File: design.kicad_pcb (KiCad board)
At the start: 2 copper layers, 60.2 x 62 mm, 32 parts, among them J1 USB_A, J2 HRO_TYPE-C-31-M-12, J3 USB_A, SW1 EN, SW2 IO9, U1 AP22804AW5, U2 AP22804AW5, U3 ESP32-C3-WROOM-02-N4, U4 MCP1700T-3302E

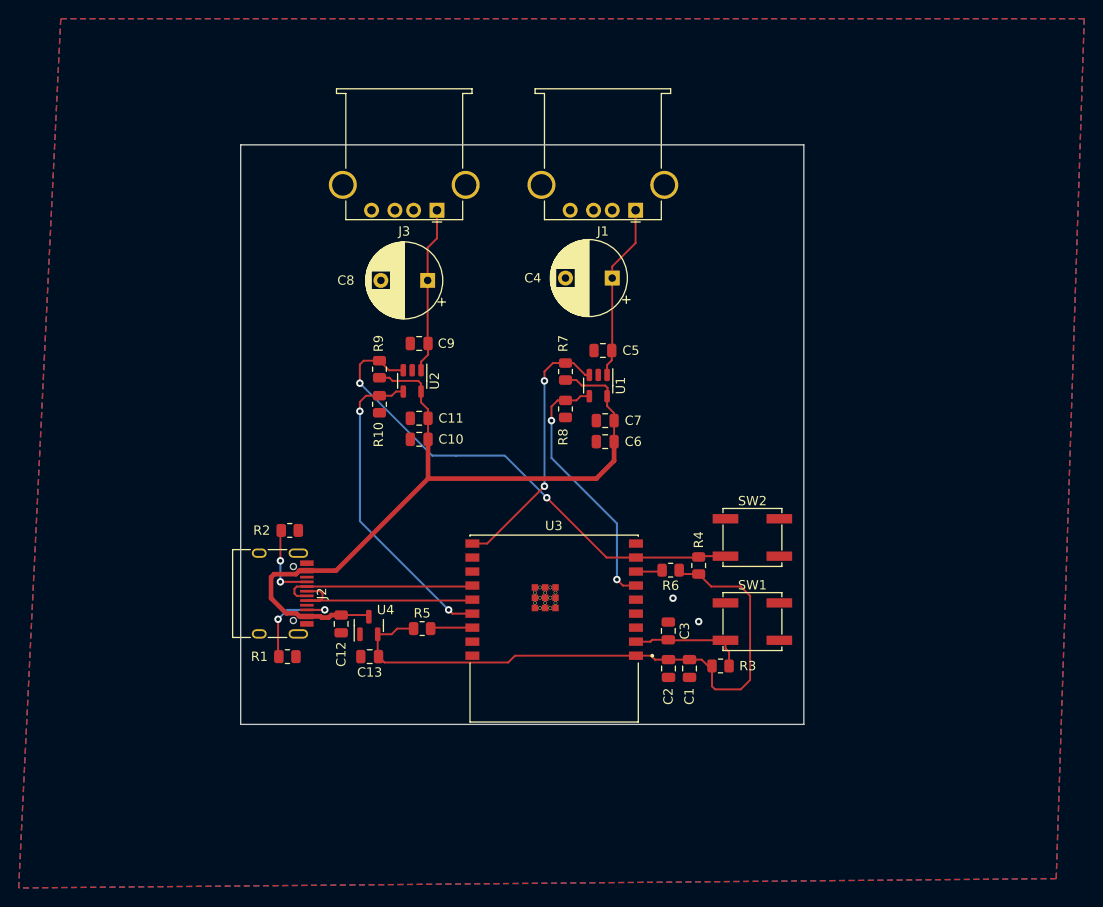
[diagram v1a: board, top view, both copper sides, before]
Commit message: add back variables for CI, rounded corners, mounting holes
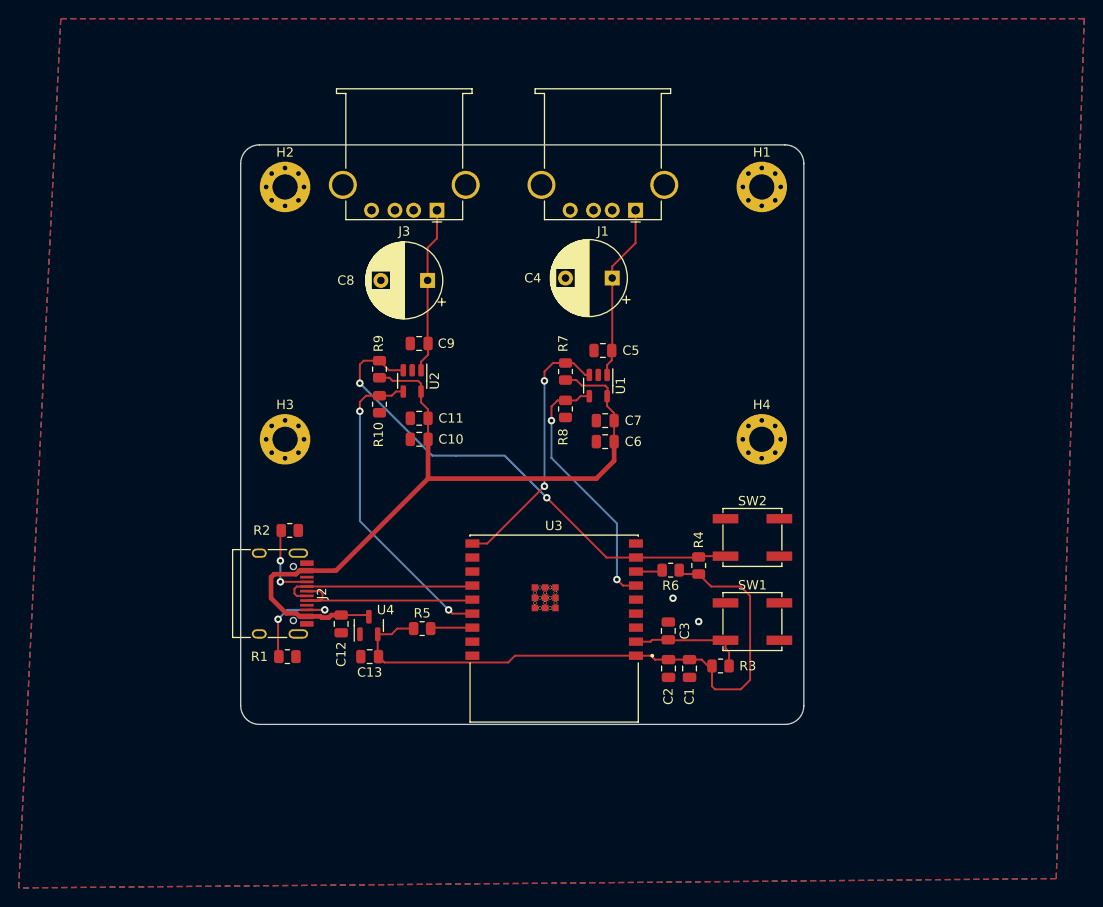
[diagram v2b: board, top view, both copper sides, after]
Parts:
- added H1: MountingHole, MountingHole:MountingHole_2.7mm_M2.5_Pad_Via, F.Cu at (180.0, 88.0)
- added H2: MountingHole, MountingHole:MountingHole_2.7mm_M2.5_Pad_Via, F.Cu at (129.0, 88.0)
- added H3: MountingHole, MountingHole:MountingHole_2.7mm_M2.5_Pad_Via, F.Cu at (129.0, 115.0)
- added H4: MountingHole, MountingHole:MountingHole_2.7mm_M2.5_Pad_Via, F.Cu at (180.0, 115.0)
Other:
- outline, holes or cut-outs redrawn
- board text added: "<<project_name>> <<ID>> <<version>> <<date>> <<hash>> <<website_link>>"
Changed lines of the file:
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@@
     )
+  )
+  (footprint "MountingHole:MountingHole_2.7mm_M2.5_Pad_Via" (layer "F.Cu")
+    (at 180 88)
+    (descr "Mounting Hole 2.7mm")
+    (tags "mounting hole 2.7mm")
+    (property "Sheetfile" "design.kicad_sch")
+    (property "Sheetname" "")
+    (attr exclude_from_pos_files)
+    (fp_text reference "H1" (at 0 -3.7) (layer "F.SilkS")
+      (effects (font (size 1 1) (thickness 0.15)))
+    )
+    (fp_text value "MountingHole" (at 0 3.7) (layer "F.Fab")
+      (effects (font (size 1 1) (thickness 0.15)))
+    )
+    (fp_text user "${REFERENCE}" (at 0 0) (layer "F.Fab")
+      (effects (font (size 1 1) (thickness 0.15)))
+    )
+    (fp_circle (center 0 0) (end 2.7 0) (layer "Cmts.User") (width 0.15) (fill none))
+    (fp_circle (center 0 0) (end 2.95 0) (layer "F.CrtYd") (width 0.05) (fill none))
+    (pad "1" thru_hole circle (at -1.431891 1.431891) (size 0.8 0.8) (drill 0.5) (layers *.Cu *.Mask))
+    (pad "1" thru_hole circle (at 2.025 0) (size 0.8 0.8) (drill 0.5) (layers *.Cu *.Mask))
+    (pad "1" thru_hole circle (at 1.431891 -1.431891) (size 0.8 0.8) (drill 0.5) (layers *.Cu *.Mask))
+    (pad "1" thru_hole circle (at 0 2.025) (size 0.8 0.8) (drill 0.5) (layers *.Cu *.Mask))
+    (pad "1" thru_hole circle (at -2.025 0) (size 0.8 0.8) (drill 0.5) (layers *.Cu *.Mask))
+    (pad "1" thru_hole circle (at 0 0) (size 5.4 5.4) (drill 2.7) (layers *.Cu *.Mask))
+    (pad "1" thru_hole circle (at 0 -2.025) (size 0.8 0.8) (drill 0.5) (layers *.Cu *.Mask))
+    (pad "1" thru_hole circle (at -1.431891 -1.431891) (size 0.8 0.8) (drill 0.5) (layers *.Cu *.Mask))
+    (pad "1" thru_hole circle (at 1.431891 1.431891) (size 0.8 0.8) (drill 0.5) (layers *.Cu *.Mask))
   )
   (footprint "Resistor_SMD:R_0805_2012Metric" (layer "F.Cu")
@@
     )
   )
+  (footprint "MountingHole:MountingHole_2.7mm_M2.5_Pad_Via" (layer "F.Cu")
+    (at 129 115)
+    (descr "Mounting Hole 2.7mm")
+    (tags "mounting hole 2.7mm")
+    (property "Sheetfile" "design.kicad_sch")
+    (property "Sheetname" "")
+    (attr exclude_from_pos_files)
+    (fp_text reference "H3" (at 0 -3.7) (layer "F.SilkS")
+      (effects (font (size 1 1) (thickness 0.15)))
+    )
+    (fp_text value "MountingHole" (at 0 3.7) (layer "F.Fab")
+      (effects (font (size 1 1) (thickness 0.15)))
+    )
+    (fp_text user "${REFERENCE}" (at 0 0) (layer "F.Fab")
+      (effects (font (size 1 1) (thickness 0.15)))
+    )
+    (fp_circle (center 0 0) (end 2.7 0) (layer "Cmts.User") (width 0.15) (fill none))
+    (fp_circle (center 0 0) (end 2.95 0) (layer "F.CrtYd") (width 0.05) (fill none))
+    (pad "1" thru_hole circle (at 1.431891 1.431891) (size 0.8 0.8) (drill 0.5) (layers *.Cu *.Mask))
+    (pad "1" thru_hole circle (at 0 -2.025) (size 0.8 0.8) (drill 0.5) (layers *.Cu *.Mask))
+    (pad "1" thru_hole circle (at -1.431891 -1.431891) (size 0.8 0.8) (drill 0.5) (layers *.Cu *.Mask))
+    (pad "1" thru_hole circle (at -1.431891 1.431891) (size 0.8 0.8) (drill 0.5) (layers *.Cu *.Mask))
+    (pad "1" thru_hole circle (at 0 2.025) (size 0.8 0.8) (drill 0.5) (layers *.Cu *.Mask))
+    (pad "1" thru_hole circle (at 2.025 0) (size 0.8 0.8) (drill 0.5) (layers *.Cu *.Mask))
+    (pad "1" thru_hole circle (at -2.025 0) (size 0.8 0.8) (drill 0.5) (layers *.Cu *.Mask))
+    (pad "1" thru_hole circle (at 0 0) (size 5.4 5.4) (drill 2.7) (layers *.Cu *.Mask))
+    (pad "1" thru_hole circle (at 1.431891 -1.431891) (size 0.8 0.8) (drill 0.5) (layers *.Cu *.Mask))
+  )
   (footprint "Button_Switch_SMD:SW_SPST_EVPBF" (layer "F.Cu")
     (at 179 134.5)
@@
       (rotate (xyz 0 0 0))
     )
+  )
+  (footprint "MountingHole:MountingHole_2.7mm_M2.5_Pad_Via" (layer "F.Cu")
+    (at 180 115)
+    (descr "Mounting Hole 2.7mm")
+    (tags "mounting hole 2.7mm")
+    (property "Sheetfile" "design.kicad_sch")
+    (property "Sheetname" "")
+    (attr exclude_from_pos_files)
+    (fp_text reference "H4" (at 0 -3.7) (layer "F.SilkS")
+      (effects (font (size 1 1) (thickness 0.15)))
+    )
+    (fp_text value "MountingHole" (at 0 3.7) (layer "F.Fab")
+      (effects (font (size 1 1) (thickness 0.15)))
+    )
+    (fp_text user "${REFERENCE}" (at 0 0) (layer "F.Fab")
+      (effects (font (size 1 1) (thickness 0.15)))
+    )
+    (fp_circle (center 0 0) (end 2.7 0) (layer "Cmts.User") (width 0.15) (fill none))
+    (fp_circle (center 0 0) (end 2.95 0) (layer "F.CrtYd") (width 0.05) (fill none))
+    (pad "1" thru_hole circle (at 1.431891 1.431891) (size 0.8 0.8) (drill 0.5) (layers *.Cu *.Mask))
+    (pad "1" thru_hole circle (at 0 0) (size 5.4 5.4) (drill 2.7) (layers *.Cu *.Mask))
+    (pad "1" thru_hole circle (at 1.431891 -1.431891) (size 0.8 0.8) (drill 0.5) (layers *.Cu *.Mask))
+    (pad "1" thru_hole circle (at 0 2.025) (size 0.8 0.8) (drill 0.5) (layers *.Cu *.Mask))
+    (pad "1" thru_hole circle (at 2.025 0) (size 0.8 0.8) (drill 0.5) (layers *.Cu *.Mask))
+    (pad "1" thru_hole circle (at -2.025 0) (size 0.8 0.8) (drill 0.5) (layers *.Cu *.Mask))
+    (pad "1" thru_hole circle (at -1.431891 -1.431891) (size 0.8 0.8) (drill 0.5) (layers *.Cu *.Mask))
+    (pad "1" thru_hole circle (at 0 -2.025) (size 0.8 0.8) (drill 0.5) (layers *.Cu *.Mask))
+    (pad "1" thru_hole circle (at -1.431891 1.431891) (size 0.8 0.8) (drill 0.5) (layers *.Cu *.Mask))
   )
   (footprint "Capacitor_SMD:C_0805_2012Metric" (layer "F.Cu")
@@
     )
   )
+  (footprint "MountingHole:MountingHole_2.7mm_M2.5_Pad_Via" (layer "F.Cu")
+    (at 129 88)
+    (descr "Mounting Hole 2.7mm")
+    (tags "mounting hole 2.7mm")
+    (property "Sheetfile" "design.kicad_sch")
+    (property "Sheetname" "")
+    (attr exclude_from_pos_files)
+    (fp_text reference "H2" (at 0 -3.7) (layer "F.SilkS")
+      (effects (font (size 1 1) (thickness 0.15)))
+    )
+    (fp_text value "MountingHole" (at 0 3.7) (layer "F.Fab")
+      (effects (font (size 1 1) (thickness 0.15)))
+    )
+    (fp_text user "${REFERENCE}" (at 0 0) (layer "F.Fab")
+      (effects (font (size 1 1) (thickness 0.15)))
+    )
+    (fp_circle (center 0 0) (end 2.7 0) (layer "Cmts.User") (width 0.15) (fill none))
+    (fp_circle (center 0 0) (end 2.95 0) (layer "F.CrtYd") (width 0.05) (fill none))
+    (pad "1" thru_hole circle (at 2.025 0) (size 0.8 0.8) (drill 0.5) (layers *.Cu *.Mask))
+    (pad "1" thru_hole circle (at -1.431891 -1.431891) (size 0.8 0.8) (drill 0.5) (layers *.Cu *.Mask))
+    (pad "1" thru_hole circle (at 0 2.025) (size 0.8 0.8) (drill 0.5) (layers *.Cu *.Mask))
+    (pad "1" thru_hole circle (at 1.431891 -1.431891) (size 0.8 0.8) (drill 0.5) (layers *.Cu *.Mask))
+    (pad "1" thru_hole circle (at 1.431891 1.431891) (size 0.8 0.8) (drill 0.5) (layers *.Cu *.Mask))
+    (pad "1" thru_hole circle (at 0 0) (size 5.4 5.4) (drill 2.7) (layers *.Cu *.Mask))
+    (pad "1" thru_hole circle (at 0 -2.025) (size 0.8 0.8) (drill 0.5) (layers *.Cu *.Mask))
+    (pad "1" thru_hole circle (at -2.025 0) (size 0.8 0.8) (drill 0.5) (layers *.Cu *.Mask))
+    (pad "1" thru_hole circle (at -1.431891 1.431891) (size 0.8 0.8) (drill 0.5) (layers *.Cu *.Mask))
+  )
   (footprint "Resistor_SMD:R_0805_2012Metric" (layer "F.Cu")
     (at 173.25 128.5 90)
@@
     )
   )
-  (gr_rect (start 124.25 83.5) (end 184.5 145.5) (layer "Edge.Cuts") (width 0.05) (fill none))
+  (gr_line (start 182.5 145.5) (end 126.25 145.5) (layer "Edge.Cuts") (width 0.05))
+  (gr_line (start 184.5 85.5) (end 184.5 143.5) (layer "Edge.Cuts") (width 0.05))
+  (gr_arc (start 184.5 143.5) (mid 183.914214 144.914214) (end 182.5 145.5) (layer "Edge.Cuts") (width 0.05))
+  (gr_line (start 124.25 143.5) (end 124.25 85.5) (layer "Edge.Cuts") (width 0.05))
+  (gr_arc (start 126.25 145.5) (mid 124.835786 144.914214) (end 124.25 143.5) (layer "Edge.Cuts") (width 0.05))
+  (gr_line (start 126.25 83.5) (end 182.5 83.5) (layer "Edge.Cuts") (width 0.05))
+  (gr_arc (start 124.25 85.5) (mid 124.835786 84.085786) (end 126.25 83.5) (layer "Edge.Cuts") (width 0.05))
+  (gr_arc (start 182.5 83.5) (mid 183.914214 84.085786) (end 184.5 85.5) (layer "Edge.Cuts") (width 0.05))
+  (gr_text "<<project_name>>\n<<ID>>\n<<version>>\n<<date>>\n<<hash>>\n<<website_link>>" (at 155.75 105.75) (layer "B.SilkS")
+    (effects (font (size 1 1) (thickness 0.15)) (justify mirror))
+  )
+  (dimension (type aligned) (layer "Dwgs.User")
+    (pts (xy 129 115) (xy 129 88))
+    (height -10)
+    (gr_text "27.0000 mm" (at 117.85 101.5 90) (layer "Dwgs.User")
+      (effects (font (size 1 1) (thickness 0.15)))
+    )
+    (format (units 3) (units_format 1) (precision 4))
+    (style (thickness 0.1) (arrow_length 1.27) (text_position_mode 0) (extension_height 0.58642) (extension_offset 0.5) keep_text_aligned)
+  )
+  (dimension (type aligned) (layer "Dwgs.User")
+    (pts (xy 180 88) (xy 129 88))
+    (height 14.999999)
+    (gr_text "51.0000 mm" (at 154.5 71.850001) (layer "Dwgs.User")
+      (effects (font (size 1 1) (thickness 0.15)))
+    )
+    (format (units 3) (units_format 1) (precision 4))
+    (style (thickness 0.1) (arrow_length 1.27) (text_position_mode 0) (extension_height 0.58642) (extension_offset 0.5) keep_text_aligned)
+  )
   (dimension (type aligned) (layer "Dwgs.User")
     (pts (xy 184.5 83.5) (xy 184.5 145.5))
